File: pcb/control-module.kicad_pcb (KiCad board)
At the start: 2 copper layers, 66.2 x 63.6 mm, 131 parts, among them J1 Screw_Terminal_01x06, J2 Conn_Coaxial, J3 USB_C_Receptacle_USB2.0_16P, J4 Micro_SD_Card, J5 Conn_ST_STDC14, J7 Conn_ST_STDC14, Q1 SiS454DN, Q2 SiS454DN, SW1 SW_DIP_x04, SW2 SW_DIP_x04, U1 TPS2116DRL, U10 MIC5504-3.3YM5, U2 USBLC6-2SC6, U3 STM32U545RETxQ, U4 MS5607-02BA, U5 LSM6DSL, U6 MCP73831-2-OT, U7 MIC5504-3.3YM5, U8 SAM-M10Q-00B, U9 STM32WL55CCUx, Y1 Crystal, Y2 Crystal_GND23

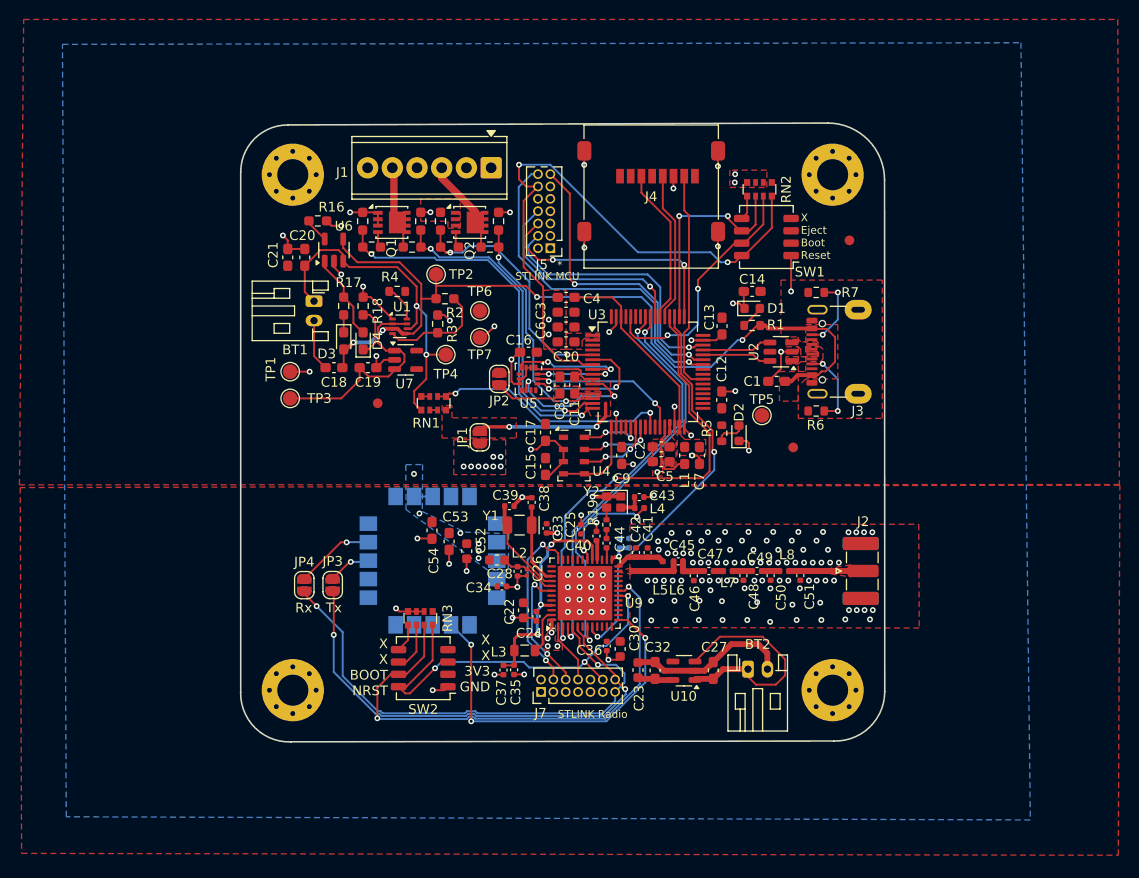
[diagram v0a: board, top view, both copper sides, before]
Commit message: Added RF Shield to layout
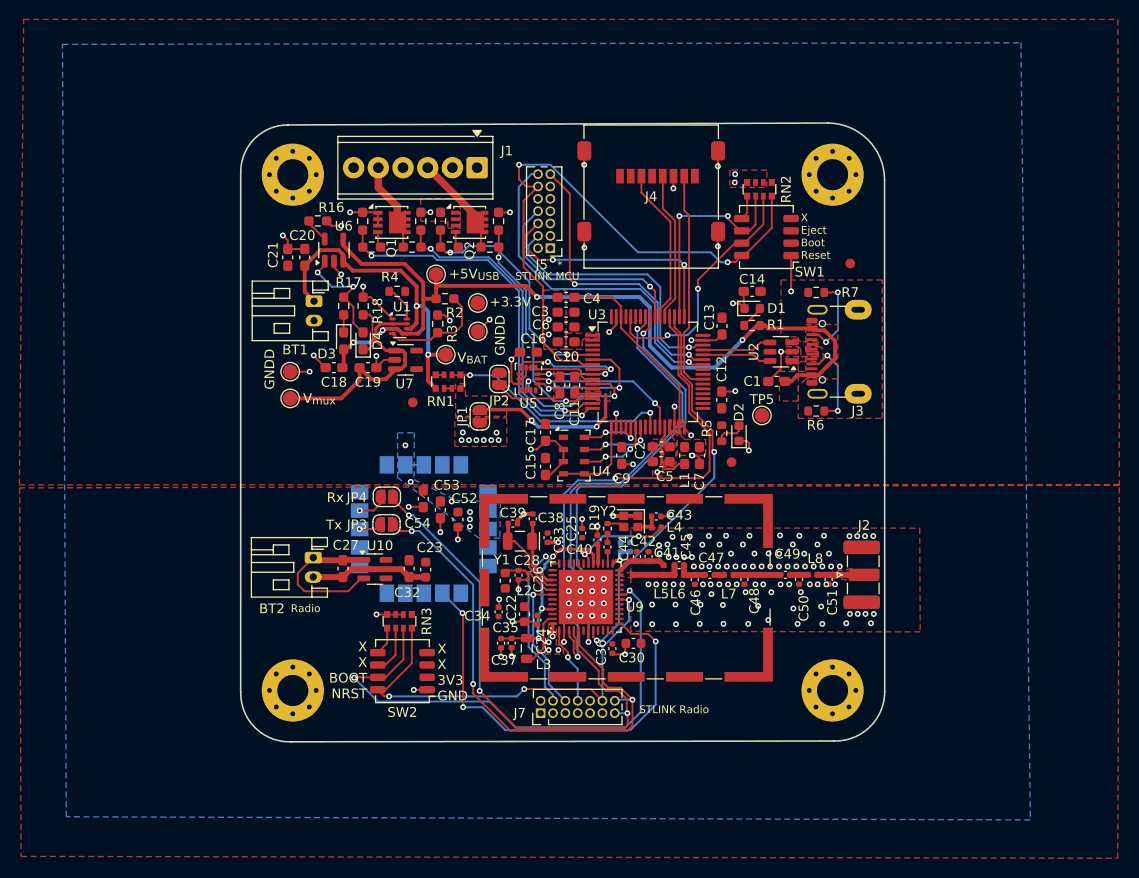
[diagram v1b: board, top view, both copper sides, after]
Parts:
- added REF**: Laird_Technologies_BMI-S-209-F_29.36x18.50mm, RF_Shielding:Laird_Technologies_BMI-S-209-F_29.36x18.50mm, F.Cu at (155.0, 74.0)
- moved BT2 46.1 mm to (122.9, 70.9), turned to -90 degrees
- moved C27 39.5 mm to (125.9, 72.0), turned to -90 degrees
- moved U10 33.5 mm to (129.2, 72.0), turned to 0 degrees
- moved C32 27.4 mm to (132.7, 72.0), turned to -90 degrees
- moved C23 24.1 mm to (134.4, 72.1), turned to -90 degrees
- moved JP4 12.4 mm to (130.4, 64.6), turned to 180 degrees
- moved JP3 8.33 mm to (130.4, 67.5), turned to 0 degrees
- moved FID2 6.52 mm to (165.9, 61.0)
- moved FID3 3.60 mm to (133.1, 54.9)
- moved C52 3.37 mm to (137.8, 67.0)
- moved C53 3.37 mm to (135.9, 66.0)
- moved C54 3.37 mm to (134.2, 64.8)
- moved U8 3.37 mm to (134.2, 67.9)
- moved C51 2.94 mm to (175.9, 73.1)
- moved C50 2.94 mm to (172.8, 73.1)
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- renumbered TP6 to +3.3V, TP2 to +5V_{USB}, TP1 to GNDD, TP7 to GNDD, TP4 to V_{BAT}, TP3 to V_{mux}
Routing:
- net GNDD: track 129.3 -> 118.7 mm, vias 171 -> 173
- net /transmitter/V_{battery_radio}: track 24.2 -> 16.4 mm
- net /Ublox_GPS_module/TIMEPULSE_OUT: track 38.5 -> 45.5 mm
- net /SPI3_MOSI: track 41.2 -> 48.1 mm
- net /Ublox_GPS_module/GPS_RX: track 8.15 -> 3.13 mm
- net /radio_TX: track 50.4 -> 54.9 mm, vias 2 -> 3
- net +3.3V_radio: track 10.5 -> 6.64 mm
- net VDDRF1V55: track 23.3 -> 19.8 mm
- net /NRST_radio: track 42.1 -> 45.2 mm
- net /radio_RX: track 52.0 -> 54.8 mm, vias 2 -> 3
- net Net-(C48-Pad1): track 1.98 -> 4.85 mm
- net /SPI3_CS: track 42.0 -> 44.8 mm
- net Net-(J2-In): track 7.54 -> 4.81 mm
- net /Battery/Status: track 8.98 -> 11.7 mm, vias 0 -> 2
- net /transmitter/BOOT0_radio: track 52.9 -> 55.5 mm
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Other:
- outline, holes or cut-outs redrawn
- board text added: "Control Module Rev. 2 Electric Boogaloo Final_Final_v2_REAL Hootenanny Core Advanced Tomfoolery Unit (ATU) Magic Smoke Containment Unit"
- board text added: "Radio"
- board text removed: "Control Module Rev. 2 Electric Boogaloo"
